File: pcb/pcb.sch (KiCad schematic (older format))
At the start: 10 parts

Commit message: added schematic for hall-effect sensor
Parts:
- removed D?: LED, SMT:0603, symbol generic:LED
- removed R?: R, SMT:0603, symbol generic:R
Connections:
- net labels added: hall_effect
- wire segments 25 -> 23
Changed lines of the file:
@@
 EESchema Schematic File Version 4
+LIBS:pcb-cache
 EELAYER 26 0
 EELAYER END
 $Descr A4 11693 8268
 encoding utf-8
-Sheet 1 2
+Sheet 1 3
 Title "Kaljajuna-veturi"
 Date ""
@@
 Connection ~ 4100 2900
 $Sheet
-S 6600 3400 1400 1300
+S 6600 3400 1000 800
 U 5E8E1E56
 F0 "Motor driver" 79
@@
 F3 "motor_drive-" I L 6600 3800 50
 $EndSheet
-$Comp
-L generic:LED D?
-U 1 1 5E8E201A
-P 5800 3200
-F 0 "D?" V 5800 3328 50  0000 L CNN
-F 1 "LED" H 5800 3100 50  0001 C CNN
-F 2 "SMT:0603" H 5810 3200 50  0001 C CNN
-F 3 "" H 5810 3200 50  0001 C CNN
-	1    5800 3200
-	0    1    1    0
-$EndComp
-$Comp
-L generic:R R?
-U 1 1 5E8E2090
-P 5600 3500
-F 0 "R?" H 5600 3402 50  0000 C CNN
-F 1 "R" H 5600 3400 50  0001 C CNN
-F 2 "SMT:0603" H 5500 3475 50  0001 C CNN
-F 3 "" H 5600 3500 50  0001 C CNN
-	1    5600 3500
-	-1   0    0    1
-$EndComp
-Wire Wire Line
-	4800 2900 5800 2900
-Wire Wire Line
-	5800 2900 5800 3100
-Connection ~ 4800 2900
-Wire Wire Line
-	5700 3500 5800 3500
-Wire Wire Line
-	5800 3500 5800 3300
-Wire Wire Line
-	5500 3500 5300 3500
 Wire Wire Line
 	5300 3700 6600 3700
@@
 Text Label 5500 3800 0    50   ~ 0
 motor_drive-
+Wire Wire Line
+	5300 3200 6100 3200
+Wire Wire Line
+	6100 3200 6100 2700
+$Sheet
+S 6600 2300 1000 800
+U 5E98F463
+F0 "Hall-effect sensor" 79
+F1 "hall-effect.sch" 50
+F2 "hall_effect" O L 6600 2700 50
+$EndSheet
+Wire Wire Line
+	6600 2700 6100 2700
+Text Label 5500 3200 0    50   ~ 0
+hall_effect
 $EndSCHEMATC

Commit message: moved motor driver away from i2c bus
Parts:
- 3V3?: symbol generic:3V3 -> pcb-rescue:3V3-generic
- IC?: symbol modules:ESP-12F -> pcb-rescue:ESP-12F-modules
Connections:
- net motor_drive+: now also IC?.6 (IO12); no longer IC?.13 (IO4)
- net motor_drive-: now also IC?.7 (IO13); no longer IC?.14 (IO5)
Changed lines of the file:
@@
 $EndDescr
 $Comp
-L modules:ESP-12F IC?
+L pcb-rescue:ESP-12F-modules IC?
 U 1 1 5E8E03B3
 P 4800 3800
@@
 $EndComp
 $Comp
-L generic:3V3 3V3?
+L pcb-rescue:3V3-generic 3V3?
 U 1 1 5E8E1283
 P 3800 2800
@@
 Connection ~ 4100 2900
 $Sheet
-S 6600 3400 1000 800
+S 6600 3600 1000 800
 U 5E8E1E56
 F0 "Motor driver" 79
 F1 "motor-driver.sch" 50
-F2 "motor_drive+" I L 6600 3700 50
-F3 "motor_drive-" I L 6600 3800 50
+F2 "motor_drive+" I L 6600 3900 50
+F3 "motor_drive-" I L 6600 4000 50
 $EndSheet
 Wire Wire Line
-	5300 3700 6600 3700
-Wire Wire Line
-	5300 3800 6600 3800
+	5300 3900 6600 3900
 $Comp
 L pin_headers:1x6 CN?
@@
 Wire Wire Line
 	3800 4300 3700 4300
-Text Label 5500 3700 0    50   ~ 0
+Text Label 5500 3900 0    50   ~ 0
 motor_drive+
-Text Label 5500 3800 0    50   ~ 0
+Text Label 5500 4000 0    50   ~ 0
 motor_drive-
 Wire Wire Line
@@
 Text Label 5500 3200 0    50   ~ 0
 hall_effect
+Wire Wire Line
+	5300 4000 6600 4000
 $EndSCHEMATC

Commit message: added resistor & capacitor values
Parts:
- C?: value C -> 1u
- R?: value R -> 10K
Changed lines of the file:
@@
 P 4100 3400
 F 0 "R?" V 4100 3453 50  0000 L CNN
-F 1 "R" H 4100 3300 50  0001 C CNN
+F 1 "10K" V 4200 3500 50  0000 C CNN
 F 2 "SMT:0603" H 4000 3375 50  0001 C CNN
 F 3 "" H 4100 3400 50  0001 C CNN
@@
 P 3800 3200
 F 0 "C?" H 3878 3200 50  0000 L CNN
-F 1 "C" H 3900 3100 50  0001 C CNN
+F 1 "1u" H 3900 3100 50  0000 C CNN
 F 2 "SMT:0603" H 3800 3100 50  0001 C CNN
 F 3 "" H 3800 3200 50  0001 C CNN

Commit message: fixed schematic symbols being rescued from cache
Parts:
- 3V3?: symbol pcb-rescue:3V3-generic -> generic:3V3
- IC?: symbol pcb-rescue:ESP-12F-modules -> modules:ESP-12F
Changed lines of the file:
@@
 $EndDescr
 $Comp
-L pcb-rescue:ESP-12F-modules IC?
+L modules:ESP-12F IC?
 U 1 1 5E8E03B3
 P 4800 3800
@@
 $EndComp
 $Comp
-L pcb-rescue:3V3-generic 3V3?
+L generic:3V3 3V3?
 U 1 1 5E8E1283
 P 3800 2800

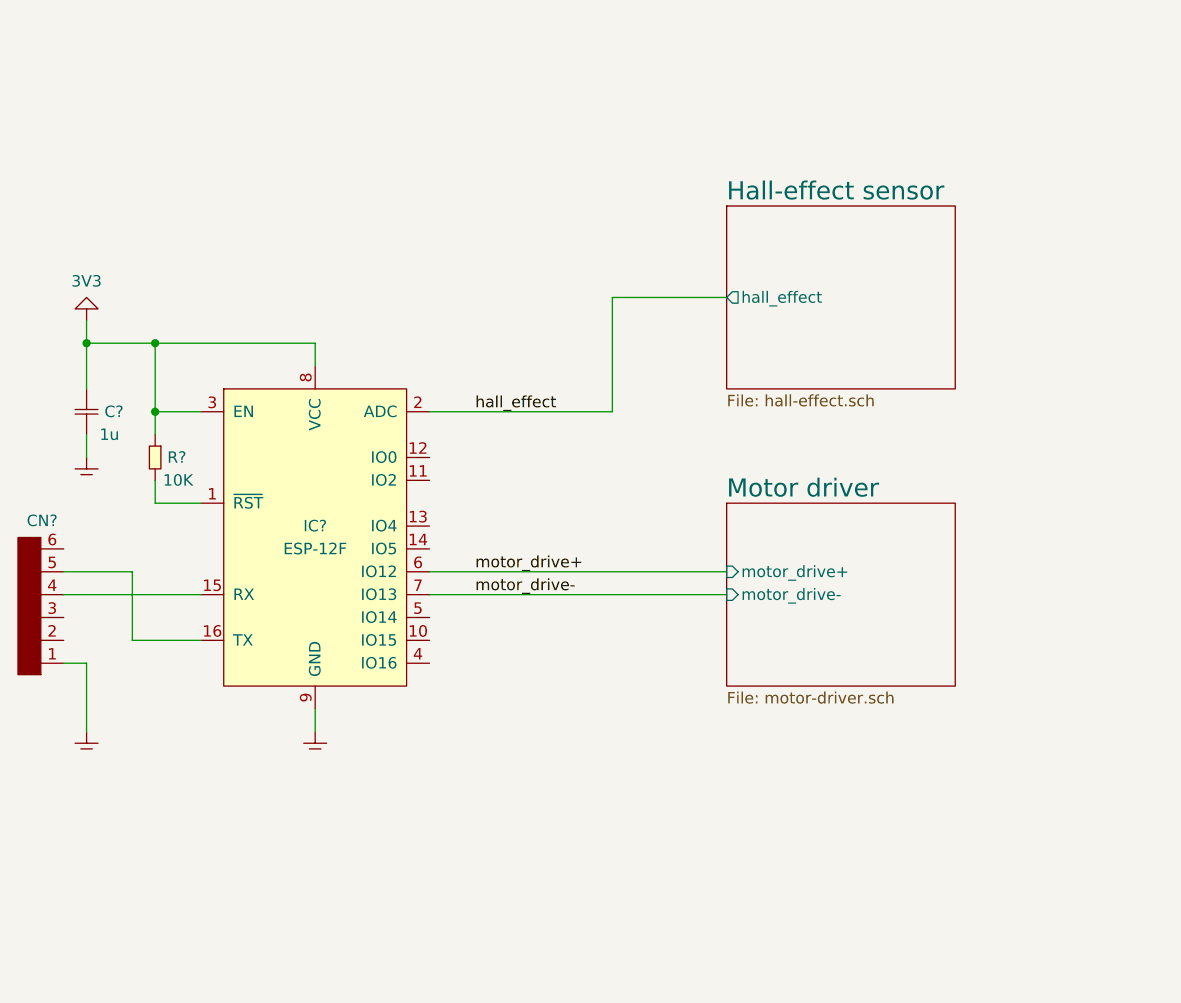
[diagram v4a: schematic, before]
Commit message: changed hall-effect circuit to use two comparators with analog inputs as triggering levels
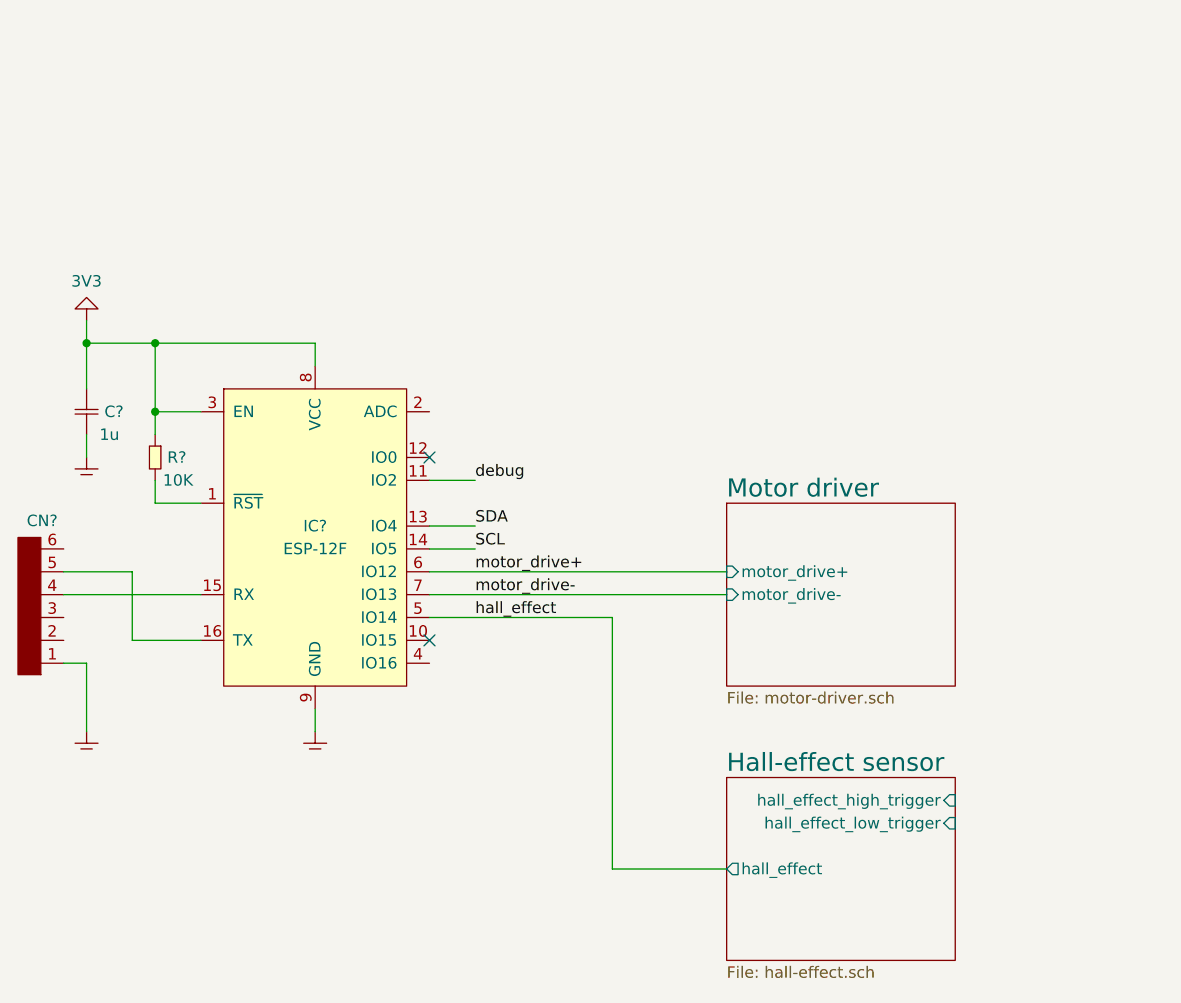
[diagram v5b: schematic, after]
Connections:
- net hall_effect: now also IC?.5 (IO14); no longer IC?.2 (ADC)
- net debug: now reaches IC?.11 (IO2)
- net SDA: now reaches IC?.13 (IO4)
- net SCL: now reaches IC?.14 (IO5)
- no-connect marks 0 -> 2
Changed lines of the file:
@@
 Text Label 5500 4000 0    50   ~ 0
 motor_drive-
-Wire Wire Line
-	5300 3200 6100 3200
-Wire Wire Line
-	6100 3200 6100 2700
 $Sheet
-S 6600 2300 1000 800
+S 6600 4800 1000 800
 U 5E98F463
 F0 "Hall-effect sensor" 79
 F1 "hall-effect.sch" 50
-F2 "hall_effect" O L 6600 2700 50
+F2 "hall_effect" O L 6600 5200 50
+F3 "hall_effect_low_trigger" I R 7600 5000 50
+F4 "hall_effect_high_trigger" I R 7600 4900 50
 $EndSheet
 Wire Wire Line
-	6600 2700 6100 2700
-Text Label 5500 3200 0    50   ~ 0
+	5300 4000 6600 4000
+Text Label 5500 3700 0    50   ~ 0
+SDA
+Text Label 5500 3800 0    50   ~ 0
+SCL
+Wire Wire Line
+	5500 3800 5300 3800
+Wire Wire Line
+	5300 3700 5500 3700
+Text Label 5500 3500 0    50   ~ 0
+debug
+Wire Wire Line
+	5300 3500 5500 3500
+NoConn ~ 5300 3400
+NoConn ~ 5300 4200
+Wire Wire Line
+	6600 5200 6100 5200
+Wire Wire Line
+	6100 5200 6100 4100
+Wire Wire Line
+	6100 4100 5300 4100
+Text Label 5500 4100 0    50   ~ 0
 hall_effect
-Wire Wire Line
-	5300 4000 6600 4000
 $EndSCHEMATC

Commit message: added DAC to schematic
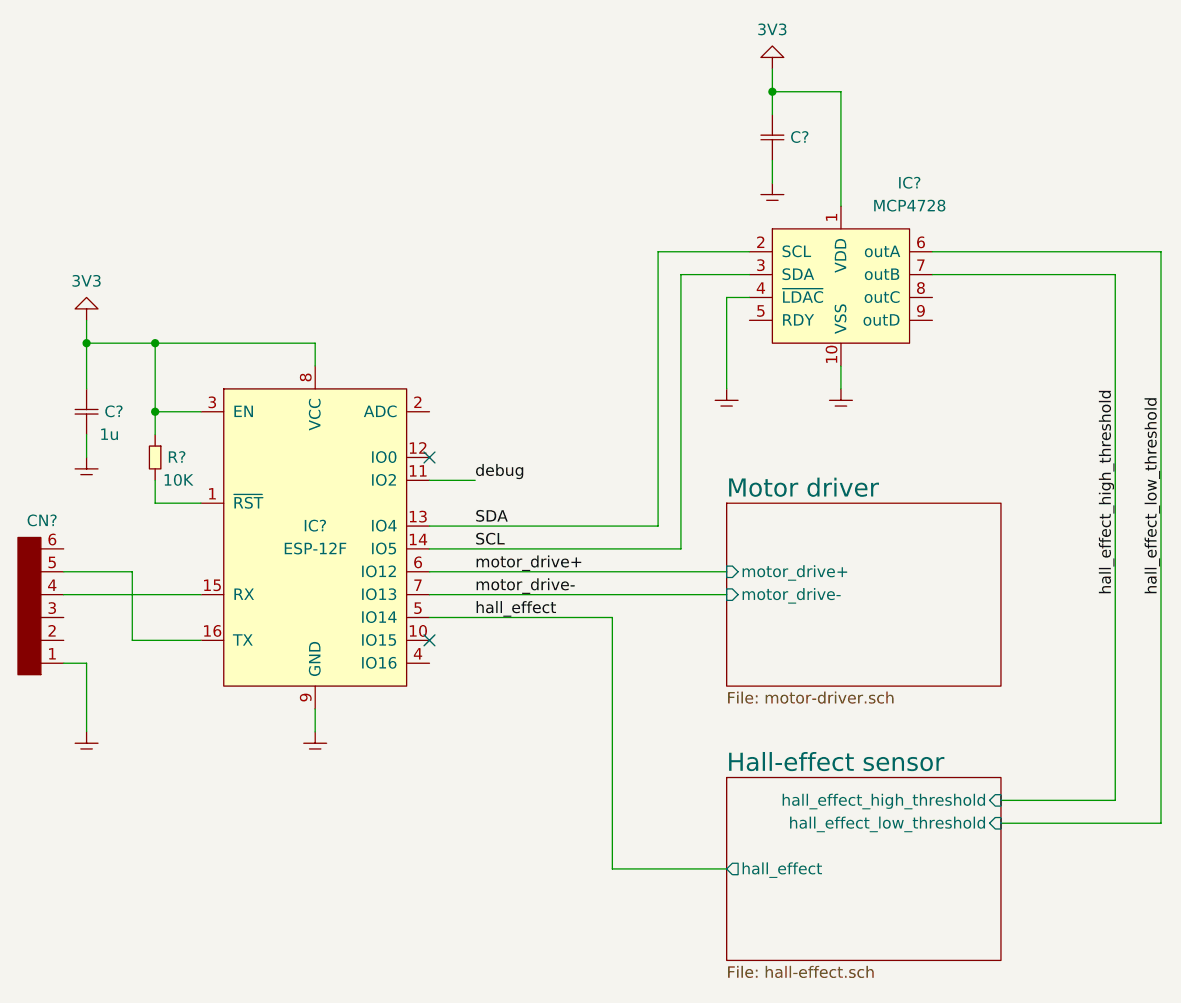
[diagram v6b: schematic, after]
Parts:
- added 3V?: 3V3, symbol generic:3V3
- added C?: C, SMT:0603, symbol generic:C
- added GND? (x3): GND, symbol generic:GND
- added IC?: MCP4728, symbol DAC:MCP4728
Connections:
- net GND: now also 3V?.~ (GND), C?.1, C?.2, GND?.~ (GND), GND?.~ (GND), GND?.~ (GND), IC?.1 (VDD), IC?.10 (VSS), IC?.4 (~LDAC)
- net SCL: now also IC?.3 (SDA)
- net SDA: now also IC?.2 (SCL)
- new net hall_effect_high_threshold: IC?.7 (outB)
- new net hall_effect_low_threshold: IC?.6 (outA)
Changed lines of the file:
@@
 Connection ~ 4100 2900
 $Sheet
-S 6600 3600 1000 800
+S 6600 3600 1200 800
 U 5E8E1E56
 F0 "Motor driver" 79
@@
 motor_drive-
 $Sheet
-S 6600 4800 1000 800
+S 6600 4800 1200 800
 U 5E98F463
 F0 "Hall-effect sensor" 79
 F1 "hall-effect.sch" 50
 F2 "hall_effect" O L 6600 5200 50
-F3 "hall_effect_low_trigger" I R 7600 5000 50
-F4 "hall_effect_high_trigger" I R 7600 4900 50
+F3 "hall_effect_low_threshold" I R 7800 5000 50
+F4 "hall_effect_high_threshold" I R 7800 4900 50
 $EndSheet
 Wire Wire Line
@@
 Text Label 5500 3800 0    50   ~ 0
 SCL
-Wire Wire Line
-	5500 3800 5300 3800
-Wire Wire Line
-	5300 3700 5500 3700
 Text Label 5500 3500 0    50   ~ 0
 debug
@@
 Text Label 5500 4100 0    50   ~ 0
 hall_effect
+$Comp
+L DAC:MCP4728 IC?
+U 1 1 5EA593A1
+P 7100 2600
+F 0 "IC?" H 7400 3000 50  0000 C CNN
+F 1 "MCP4728" H 7400 2900 50  0000 C CNN
+F 2 "" H 7100 2600 50  0001 C CNN
+F 3 "" H 7100 2600 50  0001 C CNN
+	1    7100 2600
+	1    0    0    -1
+$EndComp
+$Comp
+L generic:GND GND?
+U 1 1 5EA5975A
+P 7100 3100
+F 0 "GND?" H 7250 3150 50  0001 C CNN
+F 1 "GND" H 7250 3100 50  0001 C CNN
+F 2 "" H 7100 3100 50  0001 C CNN
+F 3 "" H 7100 3100 50  0001 C CNN
+	1    7100 3100
+	1    0    0    -1
+$EndComp
+Wire Wire Line
+	7100 3100 7100 3000
+$Comp
+L generic:C C?
+U 1 1 5EA59DC2
+P 6800 2000
+F 0 "C?" H 6878 2000 50  0000 L CNN
+F 1 "C" H 6900 1900 50  0001 C CNN
+F 2 "SMT:0603" H 6800 1900 50  0001 C CNN
+F 3 "" H 6800 2000 50  0001 C CNN
+	1    6800 2000
+	1    0    0    -1
+$EndComp
+Wire Wire Line
+	7100 2300 7100 1800
+Wire Wire Line
+	7100 1800 6800 1800
+Wire Wire Line
+	6800 1800 6800 1900
+$Comp
+L generic:GND GND?
+U 1 1 5EA5A166
+P 6800 2200
+F 0 "GND?" H 6950 2250 50  0001 C CNN
+F 1 "GND" H 6950 2200 50  0001 C CNN
+F 2 "" H 6800 2200 50  0001 C CNN
+F 3 "" H 6800 2200 50  0001 C CNN
+	1    6800 2200
+	1    0    0    -1
+$EndComp
+Wire Wire Line
+	6800 2200 6800 2100
+$Comp
+L generic:3V3 3V?
+U 1 1 5EA5AF28
+P 6800 1700
+F 0 "3V?" H 6950 1750 50  0001 C CNN
+F 1 "3V3" H 6800 1900 50  0000 C TNN
+F 2 "" H 6800 1700 50  0001 C CNN
+F 3 "" H 6800 1700 50  0001 C CNN
+	1    6800 1700
+	1    0    0    -1
+$EndComp
+Wire Wire Line
+	6800 1700 6800 1800
+Connection ~ 6800 1800
+Wire Wire Line
+	6700 2700 6600 2700
+Wire Wire Line
+	6600 2700 6600 3100
+$Comp
+L generic:GND GND?
+U 1 1 5EA5B765
+P 6600 3100
+F 0 "GND?" H 6750 3150 50  0001 C CNN
+F 1 "GND" H 6750 3100 50  0001 C CNN
+F 2 "" H 6600 3100 50  0001 C CNN
+F 3 "" H 6600 3100 50  0001 C CNN
+	1    6600 3100
+	1    0    0    -1
+$EndComp
+Wire Wire Line
+	6400 3800 6400 2600
+Wire Wire Line
+	6400 2600 6700 2600
+Wire Wire Line
+	5300 3800 6400 3800
+Wire Wire Line
+	6300 3700 6300 2500
+Wire Wire Line
+	6300 2500 6700 2500
+Wire Wire Line
+	5300 3700 6300 3700
+Wire Wire Line
+	7500 2500 8500 2500
+Wire Wire Line
+	8500 2500 8500 5000
+Wire Wire Line
+	8500 5000 7800 5000
+Wire Wire Line
+	7500 2600 8300 2600
+Wire Wire Line
+	8300 2600 8300 4900
+Wire Wire Line
+	8300 4900 7800 4900
+Text Label 8300 4000 1    50   ~ 0
+hall_effect_high_threshold
+Text Label 8500 4000 1    50   ~ 0
+hall_effect_low_threshold
 $EndSCHEMATC

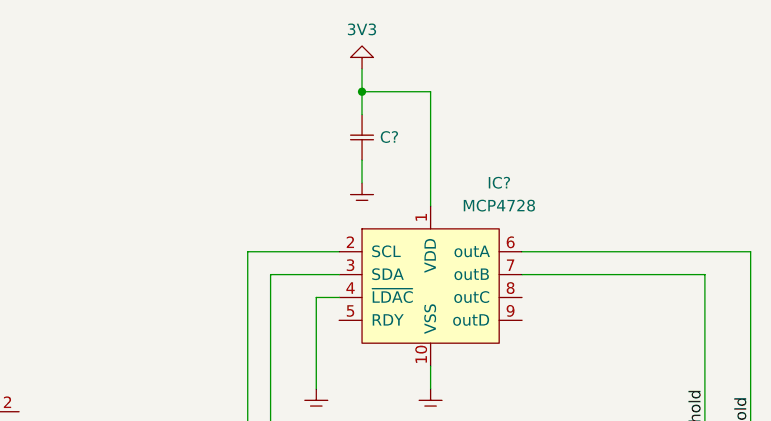
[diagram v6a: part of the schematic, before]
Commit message: added dac capacitor value
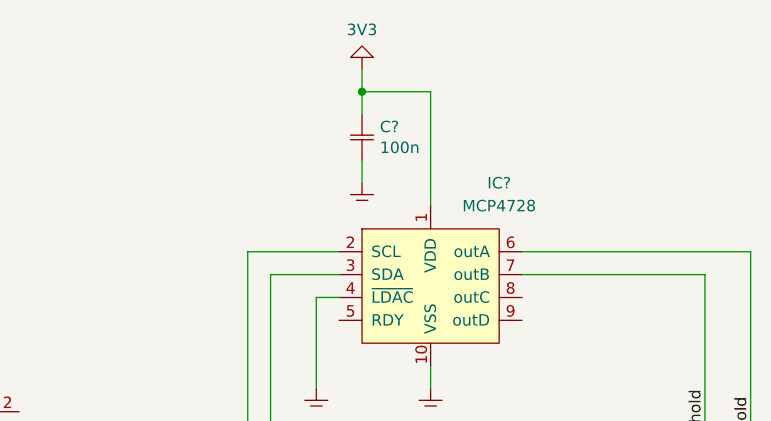
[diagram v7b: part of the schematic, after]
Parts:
- C?: value C -> 100n
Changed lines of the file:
@@
 U 1 1 5EA59DC2
 P 6800 2000
-F 0 "C?" H 6878 2000 50  0000 L CNN
-F 1 "C" H 6900 1900 50  0001 C CNN
+F 0 "C?" H 6878 2046 50  0000 L CNN
+F 1 "100n" H 6878 1955 50  0000 L CNN
 F 2 "SMT:0603" H 6800 1900 50  0001 C CNN
 F 3 "" H 6800 2000 50  0001 C CNN
